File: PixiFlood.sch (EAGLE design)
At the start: 31 parts, among them IC1 TC7W04FP-0.65, IC2 WS2811SOP8, IC3 78L05Z, U1 PT4115B89E, U2 PT4115B89E, U3 PT4115B89E, X1 22-23-2031, X2 22-23-2031

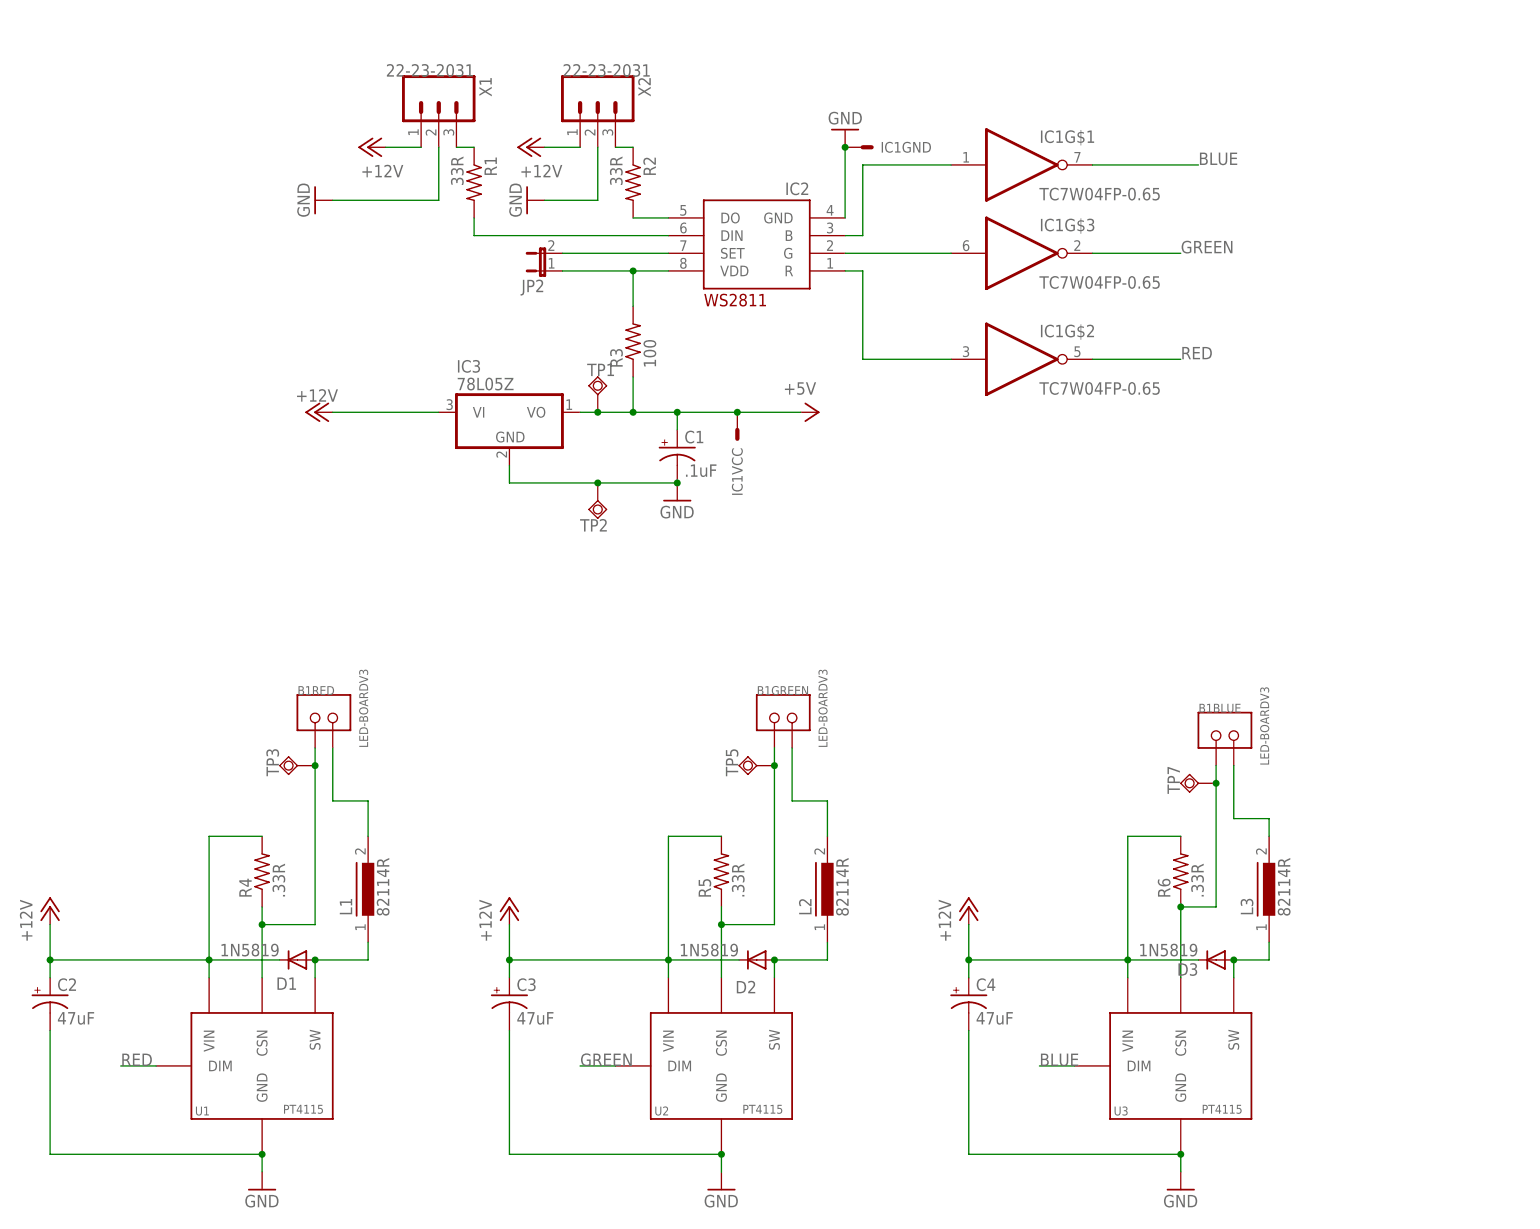
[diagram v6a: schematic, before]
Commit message: Reworked layout
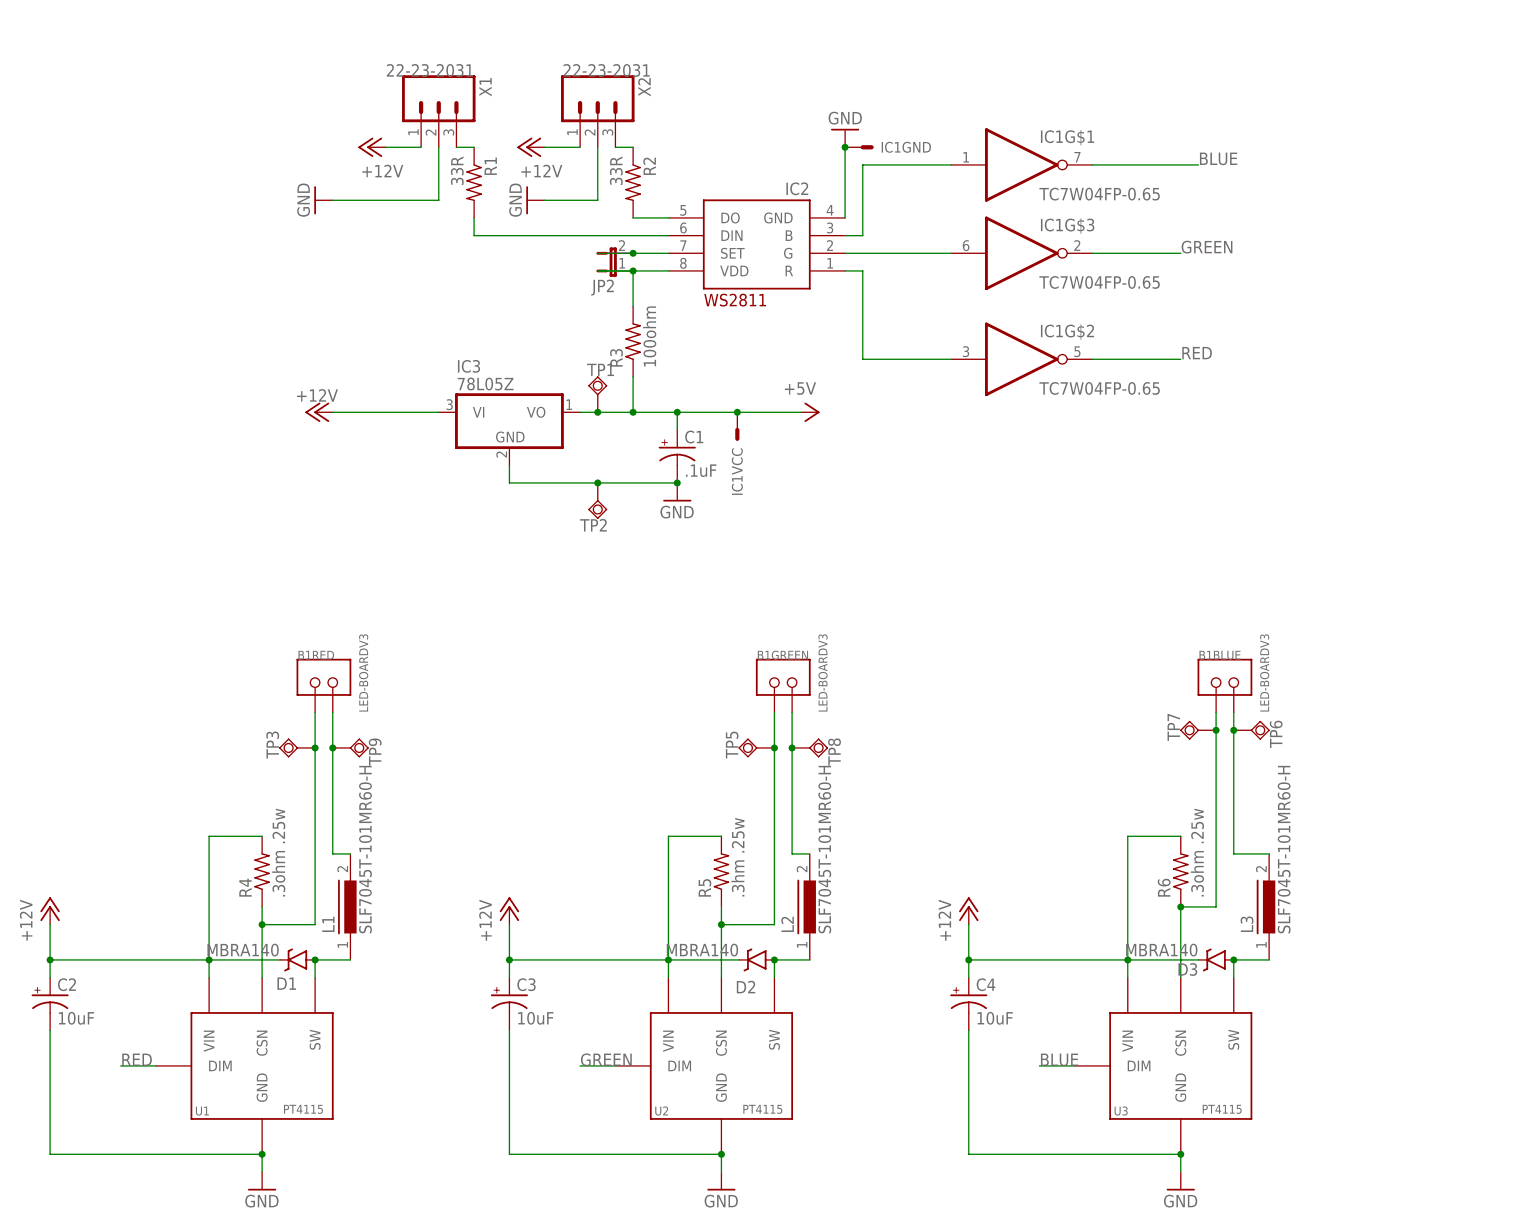
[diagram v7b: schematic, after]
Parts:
- added TP6, TP8, TP9: TPSQTP15SQ, testpad:TPSQTP15SQ
- C1: device capacitors:CAP_POLPTH50 -> capacitors:CAP_POL1206
- C2, C3, C4: value 47uF -> 10uF; device adafruit:CPOL-USE2.5-5 -> capacitors:CAP_POLCASE_D
- D1, D2, D3: value 1N5819 -> MBRA140; device diode:DIODE-DO07 -> SparkFun-DiscreteSemi:DIODE-SCHOTTKY-MBRA140
- L1, L2, L3: value 82114R -> SLF7045T-101MR60-H; device inductors:82114R -> inductors:SLF7045
- R1, R2: device rcl:R-US_0204/7 -> rcl:R-US_M1206
- R3: value 100 -> 100ohm; device rcl:R-US_0204/5 -> rcl:R-US_M1206
- R4, R6: value .33R -> .3ohm .25w; device resistor:R-US_0204/7 -> resistor:R-US_R1210
- R5: value .33R -> .3hm .25w; device resistor:R-US_0204/7 -> resistor:R-US_R1210
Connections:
- net N$10: now also TP6.TP
- net N$3: now also TP9.TP
- net N$9: now also TP8.TP
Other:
- moved on the sheet: B1BLUE, B1GREEN, B1RED, JP2, TP3, TP5, TP7

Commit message: Reworked layout
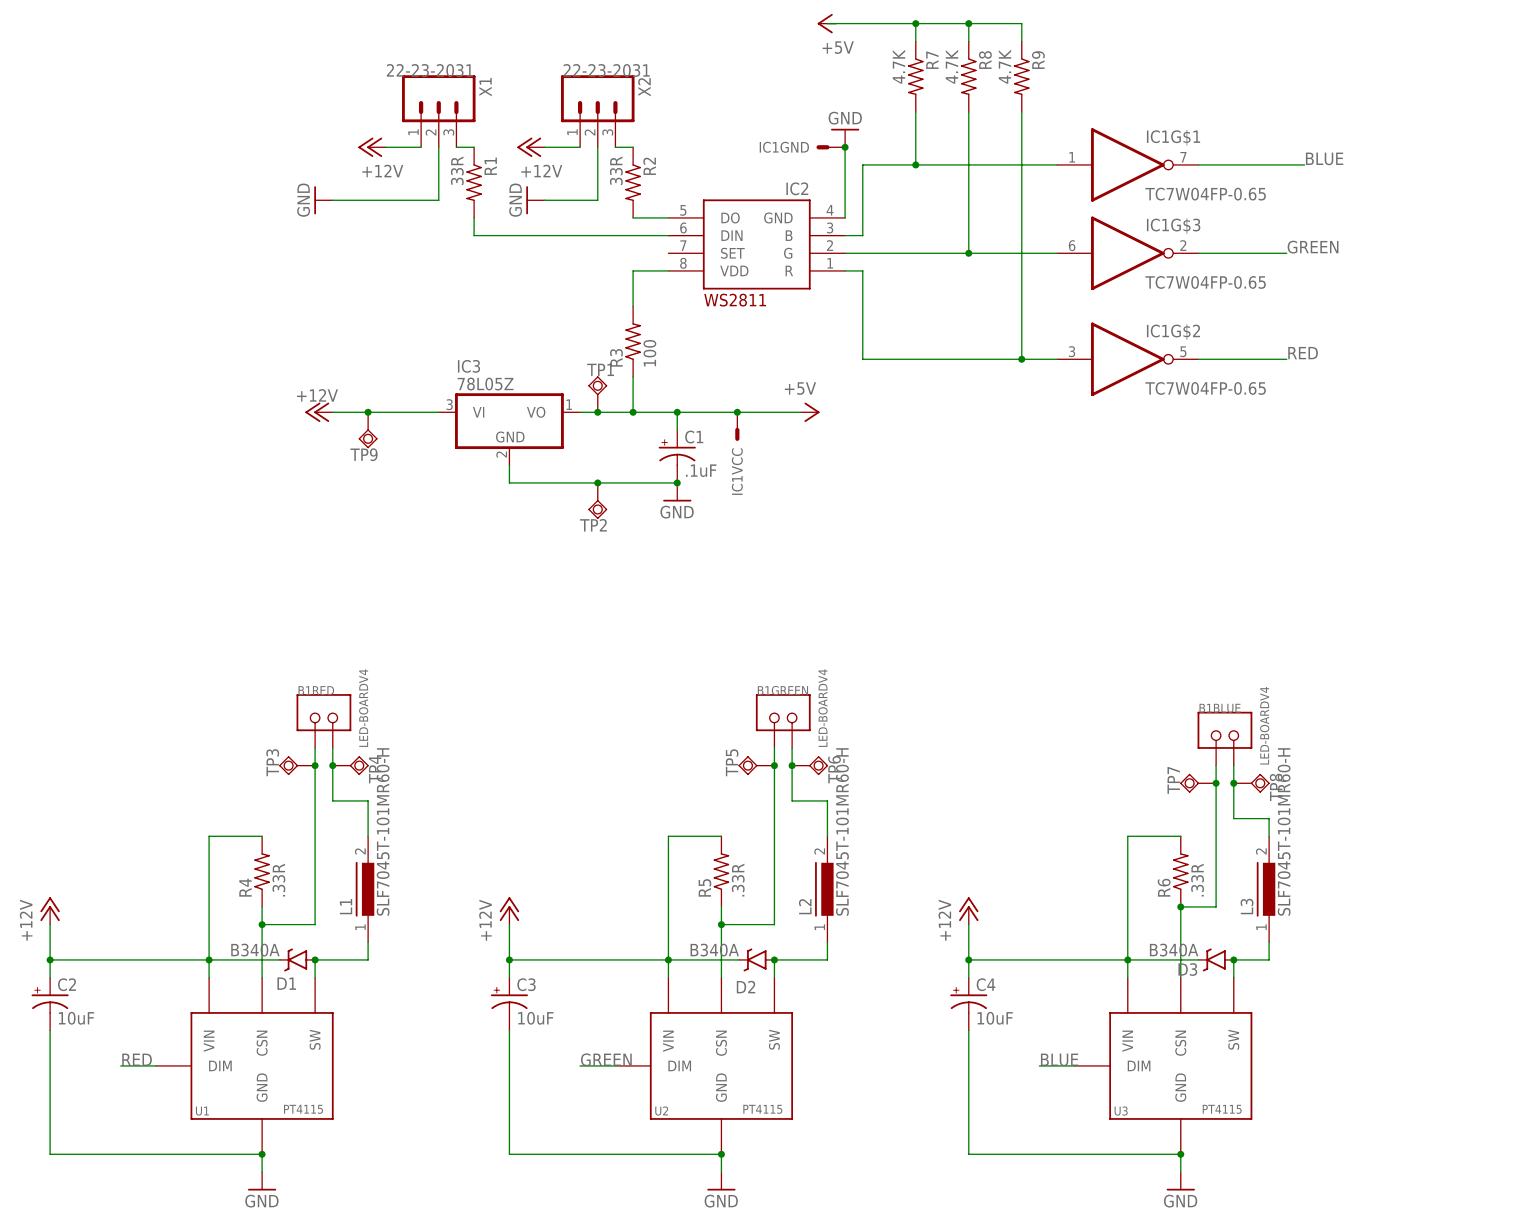
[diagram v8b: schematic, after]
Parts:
- removed JP2: (no value), jumper:JP1E
- added R7, R8, R9: 4.7K, rcl:R-US_R0805
- added TP4: TPSQTP15SQ, testpad:TPSQTP15SQ
- B1: value LED-BOARDV3 -> LED-BOARDV4; device special:LED-BOARDV3 -> special:LED-BOARDV4
- C2, C3, C4: device capacitors:CAP_POLCASE_D -> capacitors:CAP_POLCASE-D
- D1, D2, D3: value MBRA140 -> B340A; device SparkFun-DiscreteSemi:DIODE-SCHOTTKY-MBRA140 -> SparkFun-DiscreteSemi:DIODE-SCHOTTKY-B340A
- IC2: value WS2811SOP8 -> WS2811S; device drivers:WS2811SOP8 -> drivers:WS2811S
- R1, R2: device rcl:R-US_M1206 -> rcl:R-US_R1206
- R3: value 100ohm -> 100; device rcl:R-US_M1206 -> rcl:R-US_R1206
- R4, R6: value .3ohm .25w -> .33R
- R5: value .3hm .25w -> .33R
- TP9: value TPSQTP15SQ -> TPSQTP15R; device testpad:TPSQTP15SQ -> testpad:TPSQTP15R
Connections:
- net +12V: now also TP9.TP
- net N$10: now also TP8.TP; no longer TP6.TP
- net N$14: no longer JP2.1
- net N$15: now also R9.2
- net N$16: now also R7.2
- net N$18: now also R7.1, R8.1, R9.1; no longer IC2.SET, JP2.2
- net N$19: now also R8.2
- net N$3: now also TP4.TP; no longer TP9.TP
- net N$9: now also TP6.TP; no longer TP8.TP
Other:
- moved on the sheet: B1BLUE, B1GREEN, B1RED, IC1G$1, IC1G$2, IC1G$3, IC1GND, L1, L2, L3, TP3, TP5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
